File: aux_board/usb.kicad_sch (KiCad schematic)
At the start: 3 parts, among them J7 10155435-00011LF

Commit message: inching toward ordering SCI and AUX
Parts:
- renumbered J7 to J9
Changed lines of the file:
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@@
 		(dnp no)
 		(fields_autoplaced yes)
-		(property "Reference" "J7"
+		(property "Reference" "J9"
 			(at 154.94 73.66 0)
 			(effects
@@
 			(project "aux_board"
 				(path "/85134265-2435-454a-99c4-e49d8e69c5c2/490a0c5b-9225-4953-ad7a-fe6abb29cde0/de6bfa39-10b8-4e2d-af26-af25491f22bc"
+					(reference "J9")
+					(unit 1)
+				)
+				(path "/85134265-2435-454a-99c4-e49d8e69c5c2/490a0c5b-9225-4953-ad7a-fe6abb29cde0/5590b01a-e5bf-4b57-b49e-9bcea37f7d3d/0f53c388-84c5-443d-a142-2c49ef8a4676"
 					(reference "J7")
 					(unit 1)
 				)
-				(path "/85134265-2435-454a-99c4-e49d8e69c5c2/490a0c5b-9225-4953-ad7a-fe6abb29cde0/5590b01a-e5bf-4b57-b49e-9bcea37f7d3d/0f53c388-84c5-443d-a142-2c49ef8a4676"
-					(reference "J5")
+				(path "/85134265-2435-454a-99c4-e49d8e69c5c2/490a0c5b-9225-4953-ad7a-fe6abb29cde0/d0d594aa-f069-4758-ae70-ed6ba42e7e43/0f53c388-84c5-443d-a142-2c49ef8a4676"
+					(reference "J8")
 					(unit 1)
 				)
-				(path "/85134265-2435-454a-99c4-e49d8e69c5c2/490a0c5b-9225-4953-ad7a-fe6abb29cde0/d0d594aa-f069-4758-ae70-ed6ba42e7e43/0f53c388-84c5-443d-a142-2c49ef8a4676"
-					(reference "J6")
-					(unit 1)
-				)

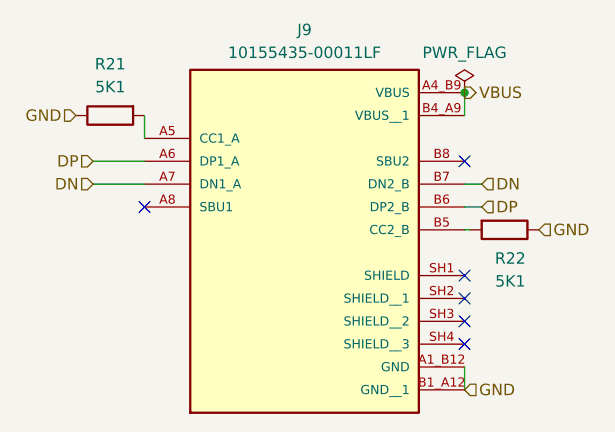
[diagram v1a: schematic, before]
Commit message: tweaking SCI and AUX for production, using common sheets as much as possible
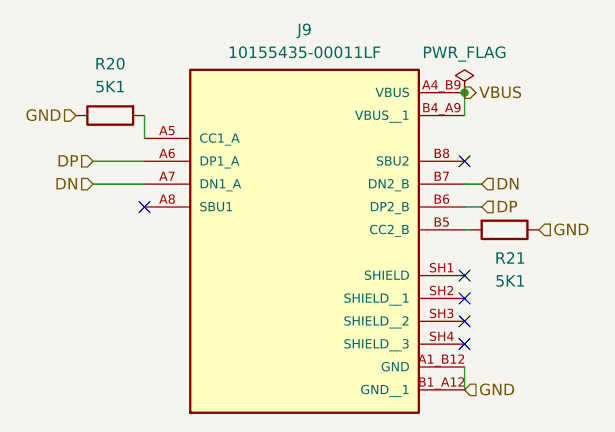
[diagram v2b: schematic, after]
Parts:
- renumbered R21 to R20, R22 to R21
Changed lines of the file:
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@@
 		(on_board yes)
 		(dnp no)
-		(property "Reference" "R22"
+		(property "Reference" "R21"
 			(at 177.8 99.06 90)
 			(effects
@@
 			(project "aux_board"
 				(path "/85134265-2435-454a-99c4-e49d8e69c5c2/490a0c5b-9225-4953-ad7a-fe6abb29cde0/de6bfa39-10b8-4e2d-af26-af25491f22bc"
-					(reference "R22")
+					(reference "R21")
 					(unit 1)
 				)
 				(path "/85134265-2435-454a-99c4-e49d8e69c5c2/490a0c5b-9225-4953-ad7a-fe6abb29cde0/5590b01a-e5bf-4b57-b49e-9bcea37f7d3d/0f53c388-84c5-443d-a142-2c49ef8a4676"
-					(reference "R14")
+					(reference "R13")
 					(unit 1)
 				)
 				(path "/85134265-2435-454a-99c4-e49d8e69c5c2/490a0c5b-9225-4953-ad7a-fe6abb29cde0/d0d594aa-f069-4758-ae70-ed6ba42e7e43/0f53c388-84c5-443d-a142-2c49ef8a4676"
-					(reference "R20")
+					(reference "R19")
 					(unit 1)
 				)
@@
 		(on_board yes)
 		(dnp no)
-		(property "Reference" "R21"
+		(property "Reference" "R20"
 			(at 133.35 77.47 90)
 			(effects
@@
 			(project "aux_board"
 				(path "/85134265-2435-454a-99c4-e49d8e69c5c2/490a0c5b-9225-4953-ad7a-fe6abb29cde0/de6bfa39-10b8-4e2d-af26-af25491f22bc"
-					(reference "R21")
+					(reference "R20")
 					(unit 1)
 				)
 				(path "/85134265-2435-454a-99c4-e49d8e69c5c2/490a0c5b-9225-4953-ad7a-fe6abb29cde0/5590b01a-e5bf-4b57-b49e-9bcea37f7d3d/0f53c388-84c5-443d-a142-2c49ef8a4676"
-					(reference "R13")
+					(reference "R12")
 					(unit 1)
 				)
 				(path "/85134265-2435-454a-99c4-e49d8e69c5c2/490a0c5b-9225-4953-ad7a-fe6abb29cde0/d0d594aa-f069-4758-ae70-ed6ba42e7e43/0f53c388-84c5-443d-a142-2c49ef8a4676"
-					(reference "R19")
+					(reference "R18")
 					(unit 1)
 				)
@@
 		(dnp no)
 		(fields_autoplaced yes)
-		(property "Reference" "#FLG06"
+		(property "Reference" "#FLG05"
 			(at 172.72 78.74 0)
 			(effects
@@
 			(project ""
 				(path "/85134265-2435-454a-99c4-e49d8e69c5c2/490a0c5b-9225-4953-ad7a-fe6abb29cde0/de6bfa39-10b8-4e2d-af26-af25491f22bc"
-					(reference "#FLG06")
+					(reference "#FLG05")
 					(unit 1)
 				)
 				(path "/85134265-2435-454a-99c4-e49d8e69c5c2/490a0c5b-9225-4953-ad7a-fe6abb29cde0/5590b01a-e5bf-4b57-b49e-9bcea37f7d3d/0f53c388-84c5-443d-a142-2c49ef8a4676"
+					(reference "#FLG03")
+					(unit 1)
+				)
+				(path "/85134265-2435-454a-99c4-e49d8e69c5c2/490a0c5b-9225-4953-ad7a-fe6abb29cde0/d0d594aa-f069-4758-ae70-ed6ba42e7e43/0f53c388-84c5-443d-a142-2c49ef8a4676"
 					(reference "#FLG04")
 					(unit 1)
 				)
-				(path "/85134265-2435-454a-99c4-e49d8e69c5c2/490a0c5b-9225-4953-ad7a-fe6abb29cde0/d0d594aa-f069-4758-ae70-ed6ba42e7e43/0f53c388-84c5-443d-a142-2c49ef8a4676"
-					(reference "#FLG05")
-					(unit 1)
-				)

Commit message: clenup BOM for SCI and AUX
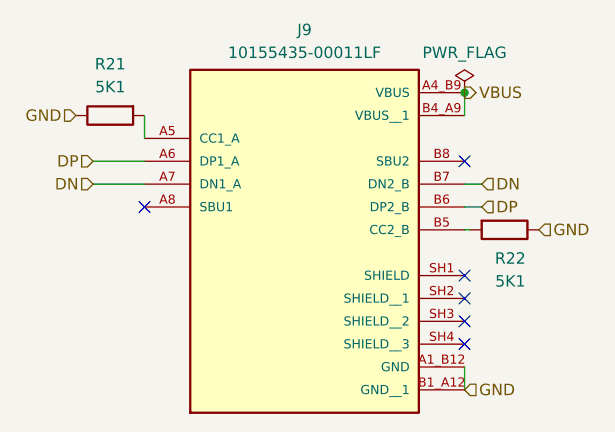
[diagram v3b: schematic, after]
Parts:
- R21: renamed from R20; footprint Resistor_SMD:R_0603_1608Metric_Pad0.98x0.95mm_HandSolder -> Resistor_SMD:R_0402_1005Metric_Pad0.72x0.64mm_HandSolder; Part Number RC0603FR-075K1L -> RC0402FR-075K1L
- R22: renamed from R21; footprint Resistor_SMD:R_0603_1608Metric_Pad0.98x0.95mm_HandSolder -> Resistor_SMD:R_0402_1005Metric_Pad0.72x0.64mm_HandSolder; Part Number RC0603FR-075K1L -> RC0402FR-075K1L
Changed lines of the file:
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@@
 		(on_board yes)
 		(dnp no)
-		(property "Reference" "R21"
+		(property "Reference" "R22"
 			(at 177.8 99.06 90)
 			(effects
@@
 			)
 		)
-		(property "Footprint" "Resistor_SMD:R_0603_1608Metric_Pad0.98x0.95mm_HandSolder"
+		(property "Footprint" "Resistor_SMD:R_0402_1005Metric_Pad0.72x0.64mm_HandSolder"
 			(at 177.165 94.107 90)
 			(effects
@@
 			)
 		)
-		(property "Part Number" "RC0603FR-075K1L"
+		(property "Part Number" "RC0402FR-075K1L"
 			(at 177.165 95.885 0)
 			(effects
@@
 		)
 		(property "Tolerance" "1"
-			(at 177.165 95.885 0)
-			(effects
-				(font
-					(size 1.27 1.27)
-				)
-				(hide yes)
-			)
-		)
-		(property "MANUFACTURER" ""
-			(at 177.165 95.885 0)
-			(effects
-				(font
-					(size 1.27 1.27)
-				)
-				(hide yes)
-			)
-		)
-		(property "MAXIMUM_PACKAGE_HEIGHT" ""
-			(at 177.165 95.885 0)
-			(effects
-				(font
-					(size 1.27 1.27)
-				)
-				(hide yes)
-			)
-		)
-		(property "Manufactorer" ""
 			(at 177.165 95.885 0)
 			(effects
@@
 			(project "aux_board"
 				(path "/85134265-2435-454a-99c4-e49d8e69c5c2/490a0c5b-9225-4953-ad7a-fe6abb29cde0/de6bfa39-10b8-4e2d-af26-af25491f22bc"
-					(reference "R21")
+					(reference "R22")
 					(unit 1)
 				)
 				(path "/85134265-2435-454a-99c4-e49d8e69c5c2/490a0c5b-9225-4953-ad7a-fe6abb29cde0/5590b01a-e5bf-4b57-b49e-9bcea37f7d3d/0f53c388-84c5-443d-a142-2c49ef8a4676"
-					(reference "R13")
+					(reference "R14")
 					(unit 1)
 				)
 				(path "/85134265-2435-454a-99c4-e49d8e69c5c2/490a0c5b-9225-4953-ad7a-fe6abb29cde0/d0d594aa-f069-4758-ae70-ed6ba42e7e43/0f53c388-84c5-443d-a142-2c49ef8a4676"
-					(reference "R19")
+					(reference "R20")
 					(unit 1)
 				)
@@
 		(on_board yes)
 		(dnp no)
-		(property "Reference" "R20"
+		(property "Reference" "R21"
 			(at 133.35 77.47 90)
 			(effects
@@
 			)
 		)
-		(property "Footprint" "Resistor_SMD:R_0603_1608Metric_Pad0.98x0.95mm_HandSolder"
+		(property "Footprint" "Resistor_SMD:R_0402_1005Metric_Pad0.72x0.64mm_HandSolder"
 			(at 133.35 81.407 90)
 			(effects
@@
 			)
 		)
-		(property "Part Number" "RC0603FR-075K1L"
+		(property "Part Number" "RC0402FR-075K1L"
 			(at 133.35 83.185 0)
 			(effects
@@
 		)
 		(property "Tolerance" "1"
-			(at 133.35 83.185 0)
-			(effects
-				(font
-					(size 1.27 1.27)
-				)
-				(hide yes)
-			)
-		)
-		(property "MANUFACTURER" ""
-			(at 133.35 83.185 0)
-			(effects
-				(font
-					(size 1.27 1.27)
-				)
-				(hide yes)
-			)
-		)
-		(property "MAXIMUM_PACKAGE_HEIGHT" ""
-			(at 133.35 83.185 0)
-			(effects
-				(font
-					(size 1.27 1.27)
-				)
-				(hide yes)
-			)
-		)
-		(property "Manufactorer" ""
 			(at 133.35 83.185 0)
 			(effects
@@
 			(project "aux_board"
 				(path "/85134265-2435-454a-99c4-e49d8e69c5c2/490a0c5b-9225-4953-ad7a-fe6abb29cde0/de6bfa39-10b8-4e2d-af26-af25491f22bc"
-					(reference "R20")
+					(reference "R21")
 					(unit 1)
 				)
 				(path "/85134265-2435-454a-99c4-e49d8e69c5c2/490a0c5b-9225-4953-ad7a-fe6abb29cde0/5590b01a-e5bf-4b57-b49e-9bcea37f7d3d/0f53c388-84c5-443d-a142-2c49ef8a4676"
-					(reference "R12")
+					(reference "R13")
 					(unit 1)
 				)
 				(path "/85134265-2435-454a-99c4-e49d8e69c5c2/490a0c5b-9225-4953-ad7a-fe6abb29cde0/d0d594aa-f069-4758-ae70-ed6ba42e7e43/0f53c388-84c5-443d-a142-2c49ef8a4676"
-					(reference "R18")
+					(reference "R19")
 					(unit 1)
 				)
@@
 		(dnp no)
 		(fields_autoplaced yes)
-		(property "Reference" "#FLG05"
+		(property "Reference" "#FLG07"
 			(at 172.72 78.74 0)
 			(effects
@@
 			(project ""
 				(path "/85134265-2435-454a-99c4-e49d8e69c5c2/490a0c5b-9225-4953-ad7a-fe6abb29cde0/de6bfa39-10b8-4e2d-af26-af25491f22bc"
-					(reference "#FLG05")
+					(reference "#FLG07")
 					(unit 1)
 				)
 				(path "/85134265-2435-454a-99c4-e49d8e69c5c2/490a0c5b-9225-4953-ad7a-fe6abb29cde0/5590b01a-e5bf-4b57-b49e-9bcea37f7d3d/0f53c388-84c5-443d-a142-2c49ef8a4676"
-					(reference "#FLG03")
+					(reference "#FLG04")
 					(unit 1)
 				)
 				(path "/85134265-2435-454a-99c4-e49d8e69c5c2/490a0c5b-9225-4953-ad7a-fe6abb29cde0/d0d594aa-f069-4758-ae70-ed6ba42e7e43/0f53c388-84c5-443d-a142-2c49ef8a4676"
-					(reference "#FLG04")
+					(reference "#FLG06")
 					(unit 1)
 				)
@@
 			)
 		)
-		(property "Description" ""
+		(property "Description" "USB-C (USB TYPE-C) Receptacle Connector 24 (16+8 Dummy) Position Surface Mount, Right Angle"
 			(at 154.94 90.805 0)
 			(effects
@@
 			(at 154.94 90.805 0)
 			(effects
-				(font
-					(size 1.27 1.27)
-				)
-				(hide yes)
-			)
-		)
-		(property "MANUFACTURER" ""
-			(at 154.94 90.805 0)
-			(effects
-				(font
-					(size 1.27 1.27)
-				)
-				(hide yes)
-			)
-		)
-		(property "MAXIMUM_PACKAGE_HEIGHT" ""
-			(at 154.94 90.805 0)
-			(effects
-				(font
-					(size 1.27 1.27)
-				)
-				(hide yes)
-			)
-		)
-		(property "Manufactorer" ""
-			(at 154.94 90.805 0)
-			(effects

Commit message: QC, add second 3V regulator to AUX, INT pullups on AUX SCI AVI
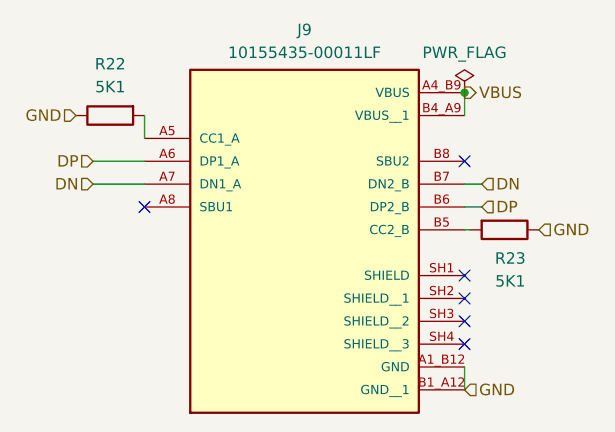
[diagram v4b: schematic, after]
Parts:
- renumbered R21 to R22, R22 to R23
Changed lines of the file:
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@@
 		(on_board yes)
 		(dnp no)
-		(property "Reference" "R22"
+		(property "Reference" "R23"
 			(at 177.8 99.06 90)
 			(effects
@@
 			(project "aux_board"
 				(path "/85134265-2435-454a-99c4-e49d8e69c5c2/490a0c5b-9225-4953-ad7a-fe6abb29cde0/de6bfa39-10b8-4e2d-af26-af25491f22bc"
-					(reference "R22")
+					(reference "R23")
 					(unit 1)
 				)
 				(path "/85134265-2435-454a-99c4-e49d8e69c5c2/490a0c5b-9225-4953-ad7a-fe6abb29cde0/5590b01a-e5bf-4b57-b49e-9bcea37f7d3d/0f53c388-84c5-443d-a142-2c49ef8a4676"
-					(reference "R14")
+					(reference "R15")
 					(unit 1)
 				)
 				(path "/85134265-2435-454a-99c4-e49d8e69c5c2/490a0c5b-9225-4953-ad7a-fe6abb29cde0/d0d594aa-f069-4758-ae70-ed6ba42e7e43/0f53c388-84c5-443d-a142-2c49ef8a4676"
-					(reference "R20")
+					(reference "R21")
 					(unit 1)
 				)
@@
 		(on_board yes)
 		(dnp no)
-		(property "Reference" "R21"
+		(property "Reference" "R22"
 			(at 133.35 77.47 90)
 			(effects
@@
 			(project "aux_board"
 				(path "/85134265-2435-454a-99c4-e49d8e69c5c2/490a0c5b-9225-4953-ad7a-fe6abb29cde0/de6bfa39-10b8-4e2d-af26-af25491f22bc"
-					(reference "R21")
+					(reference "R22")
 					(unit 1)
 				)
 				(path "/85134265-2435-454a-99c4-e49d8e69c5c2/490a0c5b-9225-4953-ad7a-fe6abb29cde0/5590b01a-e5bf-4b57-b49e-9bcea37f7d3d/0f53c388-84c5-443d-a142-2c49ef8a4676"
-					(reference "R13")
+					(reference "R14")
 					(unit 1)
 				)
 				(path "/85134265-2435-454a-99c4-e49d8e69c5c2/490a0c5b-9225-4953-ad7a-fe6abb29cde0/d0d594aa-f069-4758-ae70-ed6ba42e7e43/0f53c388-84c5-443d-a142-2c49ef8a4676"
-					(reference "R19")
-					(unit 1)
-				)
+					(reference "R20")
+					(unit 1)
+				)
